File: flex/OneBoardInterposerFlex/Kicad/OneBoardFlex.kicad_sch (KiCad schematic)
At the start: 28 parts, among them J1 GT-USB-7010ASV, SW1 TS-1187A-C-A-B, U1 RT9013-33GB-MS, U3 W25Q16JVUXIQ, U4 RP2040, Y1 ABM8-272-T3

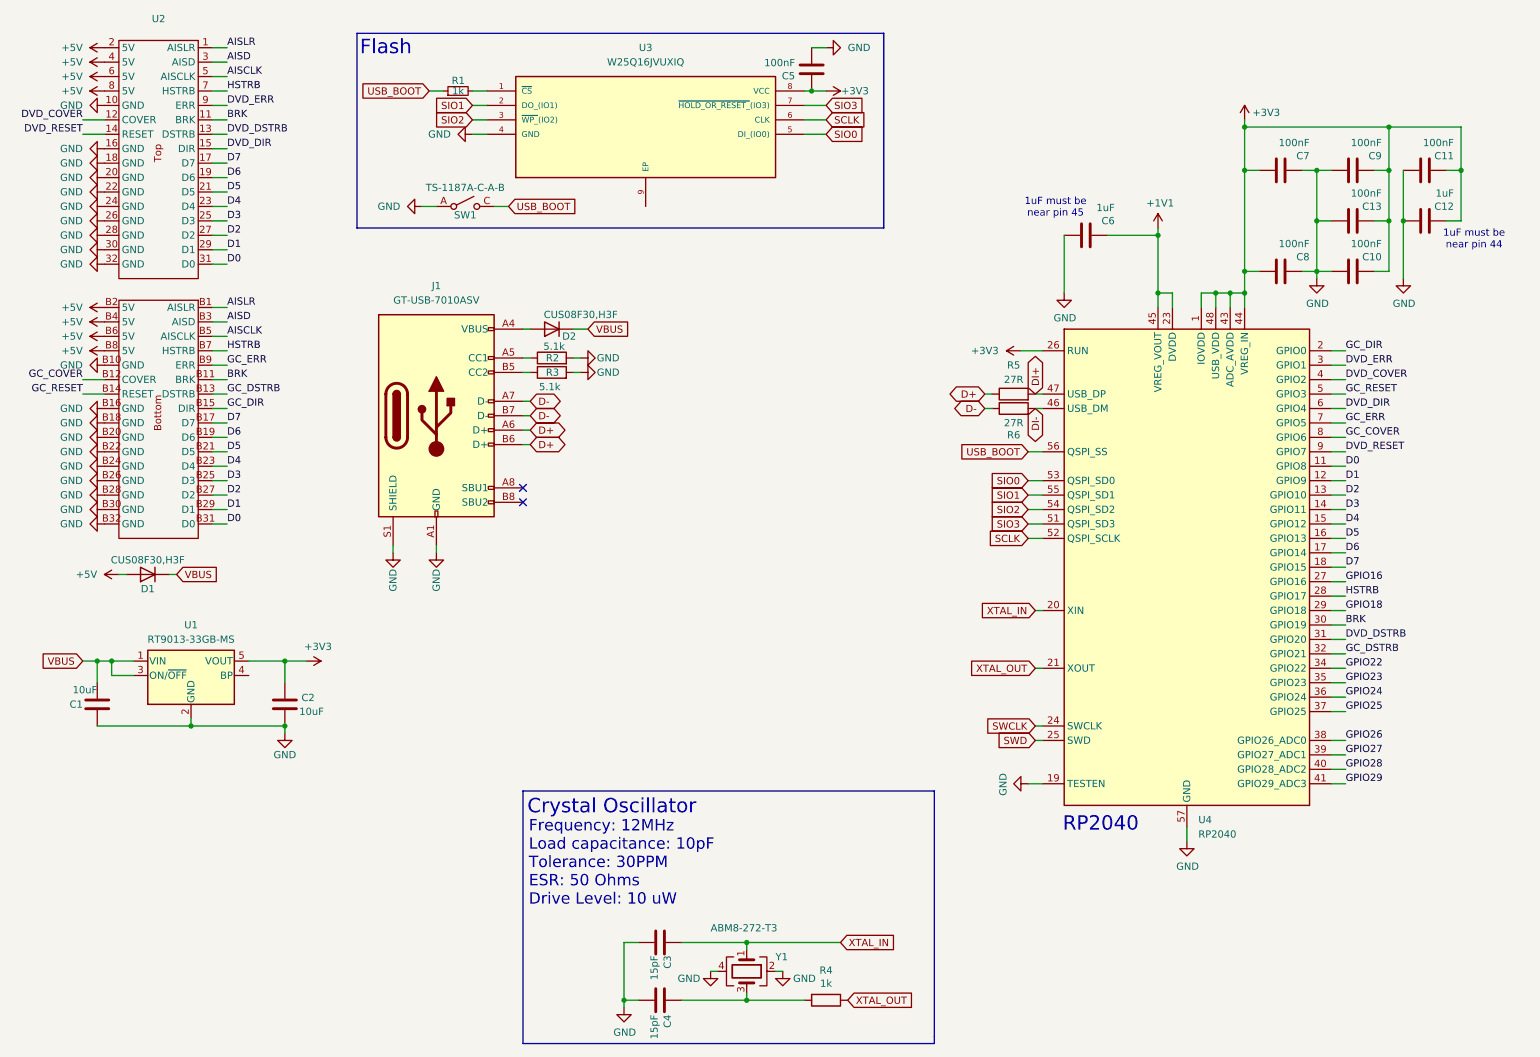
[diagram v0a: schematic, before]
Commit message: Update board per suggested changes
- Replace components with JLCPCB basic components where possible
- Implement Red LED for GPIO25
- Adjust revision to Rev1.0
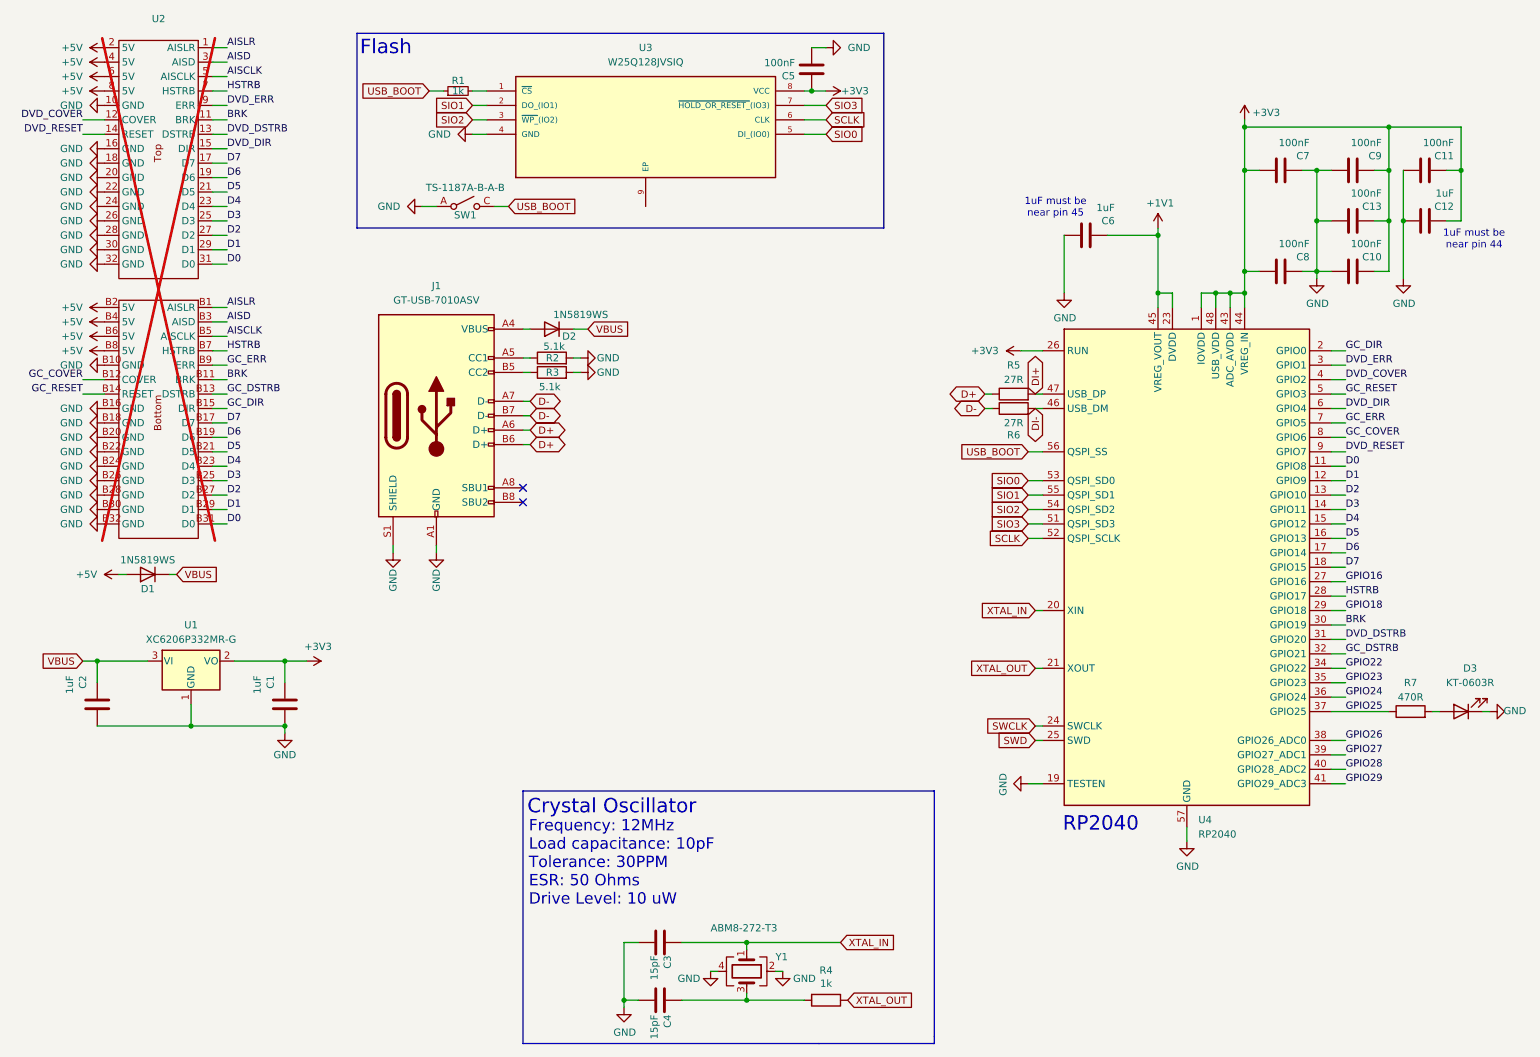
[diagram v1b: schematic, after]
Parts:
- added D3: KT-0603R, LED_SMD:LED_0603_1608Metric, symbol Device:LED
- added R7: 470R, Resistor_SMD:R_0402_1005Metric, symbol Device:R
- C1, C2: value 10uF -> 1uF; footprint Capacitor_SMD:C_0805_2012Metric -> Capacitor_SMD:C_0402_1005Metric; Confirmed (none) -> YES; JLCPN (none) -> C52923; LCSC C17024 -> (none); Link (none) -> https://jlcpcb.com/partdetail/53938-CL05A105KA5NQNC/C52923; MPN CL21A106KPFNNNE -> GRM033R60J105KEA2D; Manufacturer Samsung Electro-Mechanics -> (none); Package 0805 -> 0402; Price 0.0050 -> 0.0007
- C10, C11, C13, C7, C8, C9: footprint Capacitor_SMD:C_0201_0603Metric -> Capacitor_SMD:C_0402_1005Metric; JLCPN (none) -> C1525; LCSC C160831 -> (none); Link https://www.lcsc.com/product-detail/Multilayer-Ceramic-Capa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 -> https://jlcpcb.com/partdetail/1877-CL05B104KO5NNNC/C1525; Manufacturer Samsung Electro-Mechanics -> (none); Package 0201 -> 0402
- C12, C6: footprint Capacitor_SMD:C_0201_0603Metric -> Capacitor_SMD:C_0402_1005Metric; JLCPN (none) -> C52923; LCSC C76929 -> (none); Link https://www.lcsc.com/product-detail/Multilayer-Ceramic-Capa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 -> https://jlcpcb.com/partdetail/53938-CL05A105KA5NQNC/C52923; Manufacturer Murata Electronics -> (none); Package 0201 -> 0402
- C3, C4: JLCPN (none) -> C1548; LCSC C326803 -> (none); Link https://www.lcsc.com/product-detail/Multilayer-Ceramic-Capa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 -> https://jlcpcb.com/partdetail/1900-0402CG150J500NT/C1548; Manufacturer YAGEO -> (none)
- C5: footprint Capacitor_SMD:C_0201_0603Metric -> Capacitor_SMD:C_0402_1005Metric; JLCPN (none) -> C1525; LCSC C160831 -> (none); Link (none) -> https://jlcpcb.com/partdetail/1877-CL05B104KO5NNNC/C1525; Manufacturer Samsung Electro-Mechanics -> (none); Package 0201 -> 0402
- D1, D2: value CUS08F30,H3F -> 1N5819WS; footprint Diode_SMD:D_SOD-323_HandSoldering -> Diode_SMD:D_SOD-323; JLCPN (none) -> C191023; LCSC C150183 -> (none); Link (none) -> https://jlcpcb.com/partdetail/GuangdongHottech-1N5819WS/C19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; Manufacturer TOSHIBA -> (none)
- J1: JLCPN (none) -> C2988369; LCSC C2988369 -> (none); Link (none) -> https://jlcpcb.com/partdetail/GSwitch-GT_USB7010ASV/C2988369; Package (none) -> SMD
- R1: footprint Resistor_SMD:R_0201_0603Metric -> Resistor_SMD:R_0402_1005Metric; JLCPN (none) -> C11702; LCSC C138165 -> (none); Link (none) -> https://jlcpcb.com/partdetail/12256-0402WGF1001TCE/C11702; Manufacturer YAGEO -> (none); Package 0201 -> 0402
- R2, R3: footprint Resistor_SMD:R_0201_0603Metric -> Resistor_SMD:R_0402_1005Metric; JLCPN (none) -> C25905; LCSC C274341 -> (none); Link (none) -> https://jlcpcb.com/partdetail/26648-0402WGF5101TCE/C25905; Manufacturer YAGEO -> (none); Package 0201 -> 0402
- R4: footprint Resistor_SMD:R_0201_0603Metric -> Resistor_SMD:R_0402_1005Metric; JLCPN (none) -> C11702; LCSC C138165 -> (none); Link https://www.lcsc.com/product-detail/Chip-Resistor-Surface-M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 -> https://jlcpcb.com/partdetail/12256-0402WGF1001TCE/C11702; Manufacturer YAGEO -> (none); Package 0201 -> 0402
- R5, R6: footprint Resistor_SMD:R_0201_0603Metric -> Resistor_SMD:R_0402_1005Metric; JLCPN (none) -> C138021; LCSC C273268 -> (none); Link https://www.lcsc.com/product-detail/Chip-Resistor-Surface-M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 -> https://jlcpcb.com/partdetail/YAGEO-RC0402FR0727RL/C138021; Manufacturer YAGEO -> (none); Package 0201 -> 0402
- SW1: value TS-1187A-C-A-B -> TS-1187A-B-A-B; JLCPN (none) -> C318884; LCSC C318887 -> (none); Link https://www.lcsc.com/product-detail/Tactile-Switches_XKB-Co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 -> https://jlcpcb.com/partdetail/XKBConnection-TS_1187A_B_AB/C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; Manufacturer XKB Connection -> (none)
- U1: value RT9013-33GB-MS -> XC6206P332MR-G; footprint Package_TO_SOT_SMD:SOT-23-5 -> Package_TO_SOT_SMD:SOT-23-3; symbol Regulator_Linear:LP2985-2.5 -> Regulator_Linear:XC6206PxxxMR; JLCPN (none) -> C5446; LCSC C7434207 -> (none); Link (none) -> https://jlcpcb.com/partdetail/TorexSemicon-XC6206P332MRG/C5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; Package (none) -> SOT-23-3L
- U2: now not fitted
- U3: value W25Q16JVUXIQ -> W25Q128JVSIQ; footprint hhl:USON-8-EP(2x3) -> Package_SO:SOIC-8_5.3x5.3mm_P1.27mm; JLCPN (none) -> C97521; LCSC C2843335 -> (none); Link (none) -> https://jlcpcb.com/partdetail/WinbondElec-W25Q128JVSIQ/C975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; Package (none) -> SOIC-8-208mil
- U4: JLCPN (none) -> C2040; LCSC C2040 -> (none); Link https://www.lcsc.com/product-detail/Microcontrollers-MCU-MP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 -> https://jlcpcb.com/partdetail/RaspberryPi-RP2040/C2040; Manufacturer Raspberry Pi -> (none)
- Y1: JLCPN (none) -> C20625731; LCSC C20625731 -> (none); Link https://www.lcsc.com/product-detail/Crystals_Abracon-LLC-AB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 -> https://jlcpcb.com/partdetail/AbraconLLC-ABM8_272T3/C206257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; Manufacturer Abracon LLC -> (none)
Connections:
- net +3V3: now also C1.2, U1.2 (VO); no longer C2.1, U1.5 (VOUT)
- net GND: now also C2.1, U1.1 (GND), D3.1 (K); no longer C2.2, U1.2 (GND)
- net GPIO25: now also R7.1
- net VBUS: now also C2.2; no longer C1.2, U1.1 (VIN)
- new net: D3.2 (A), R7.2

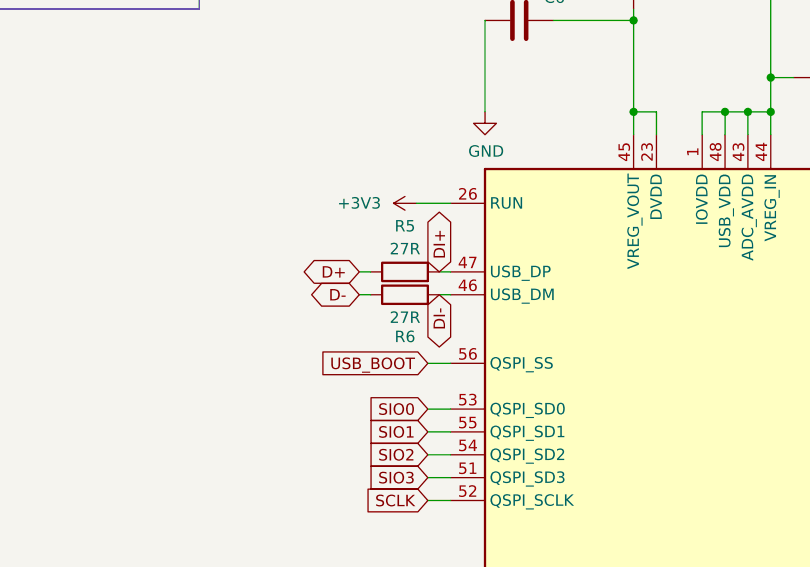
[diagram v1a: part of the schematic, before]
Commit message: 27ohm -> 22 ohm for USB resistors
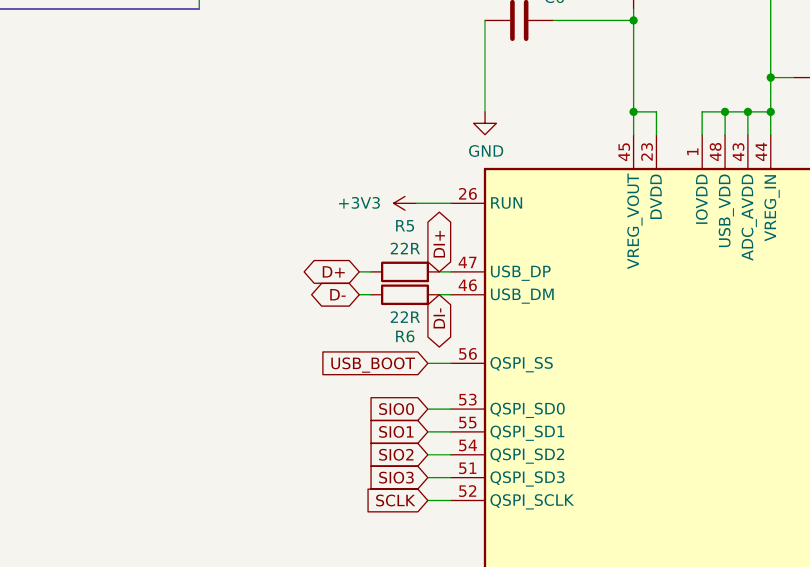
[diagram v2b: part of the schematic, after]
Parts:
- R5, R6: value 27R -> 22R; JLCPN C138021 -> C25092; Link https://jlcpcb.com/partdetail/YAGEO-RC0402FR0727RL/C138021 -> https://jlcpcb.com/partdetail/25835-0402WGF220JTCE/C25092
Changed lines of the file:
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@@
 			)
 		)
-		(property "Value" "27R"
+		(property "Value" "22R"
 			(at 189.23 86.36 90)
 			(effects
@@
 			)
 		)
-		(property "Datasheet" "https://jlcpcb.com/api/file/downloadByFileSystemAccessId/8588899757724995584"
+		(property "Datasheet" "https://jlcpcb.com/api/file/downloadByFileSystemAccessId/8579705910383595520"
 			(at 189.23 83.82 0)
 			(effects
@@
 			)
 		)
-		(property "JLCPN" "C138021"
+		(property "JLCPN" "C25092"
 			(at 189.23 83.82 0)
 			(effects
@@
 			)
 		)
-		(property "Link" "https://jlcpcb.com/partdetail/YAGEO-RC0402FR0727RL/C138021"
+		(property "Link" "https://jlcpcb.com/partdetail/25835-0402WGF220JTCE/C25092"
 			(at 189.23 83.82 0)
 			(effects
@@
 			)
 		)
-		(property "Value" "27R"
+		(property "Value" "22R"
 			(at 189.23 78.74 90)
 			(effects
@@
 			)
 		)
-		(property "Datasheet" "https://jlcpcb.com/api/file/downloadByFileSystemAccessId/8588899757724995584"
+		(property "Datasheet" "https://jlcpcb.com/api/file/downloadByFileSystemAccessId/8579705910383595520"
 			(at 189.23 81.28 0)
 			(effects
@@
 			)
 		)
-		(property "JLCPN" "C138021"
+		(property "JLCPN" "C25092"
 			(at 189.23 81.28 0)
 			(effects
@@
 			)
 		)
-		(property "Link" "https://jlcpcb.com/partdetail/YAGEO-RC0402FR0727RL/C138021"
-			(at 189.23 81.28 0)
-			(effects
+		(property "Link" "https://jlcpcb.com/partdetail/25835-0402WGF220JTCE/C25092"
+			(at 189.23 81.28 0)
+			(effects
